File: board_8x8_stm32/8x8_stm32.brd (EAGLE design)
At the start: 100 x 100 mm, 127 parts, among them IC1 STM32F0, J1 SWD_SHROUD, Q1 BSS123, Q10 BSS84, Q11 BSS84, Q12 BSS84, Q13 BSS84, Q14 BSS84, Q15 BSS84, Q16 BSS84, Q2 BSS123, Q3 BSS123, Q4 BSS123, Q5 BSS123, Q6 BSS123, Q7 BSS123, Q8 BSS123, Q9 BSS84

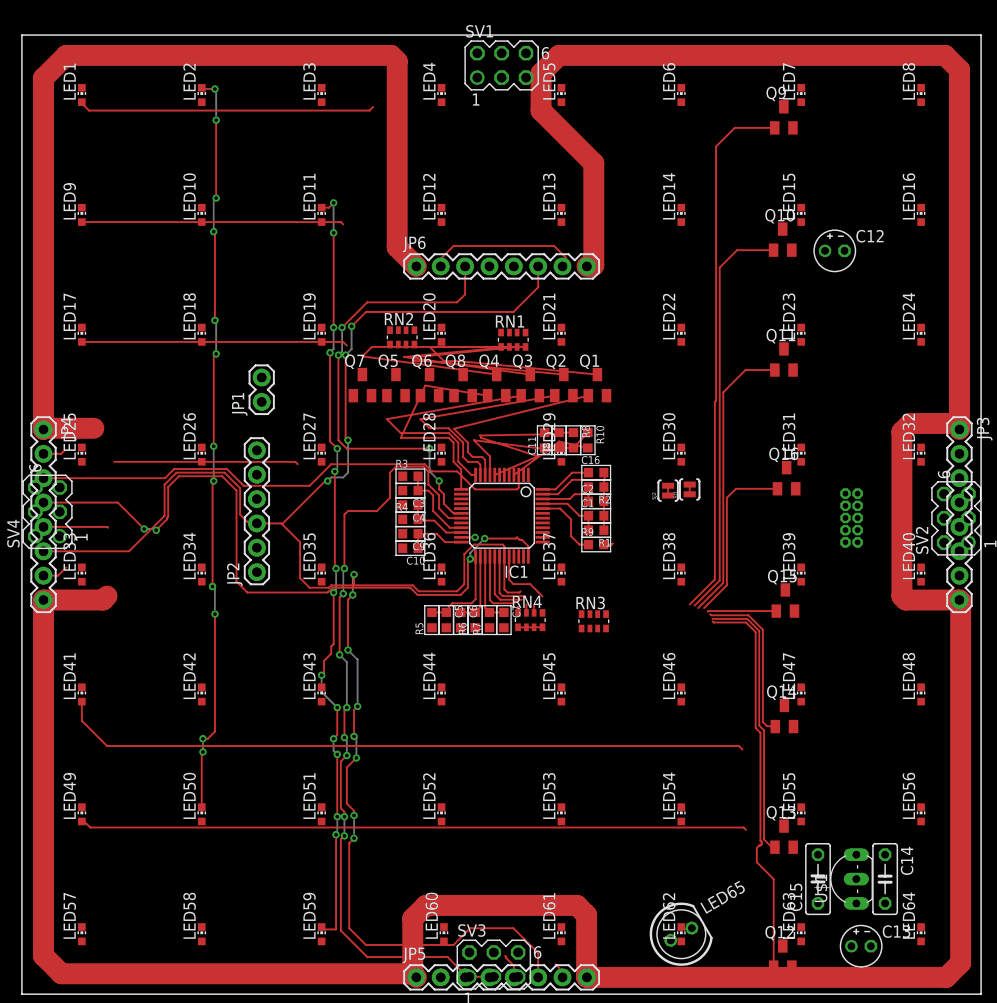
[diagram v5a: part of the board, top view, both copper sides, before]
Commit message: chnaging to combined led footprint
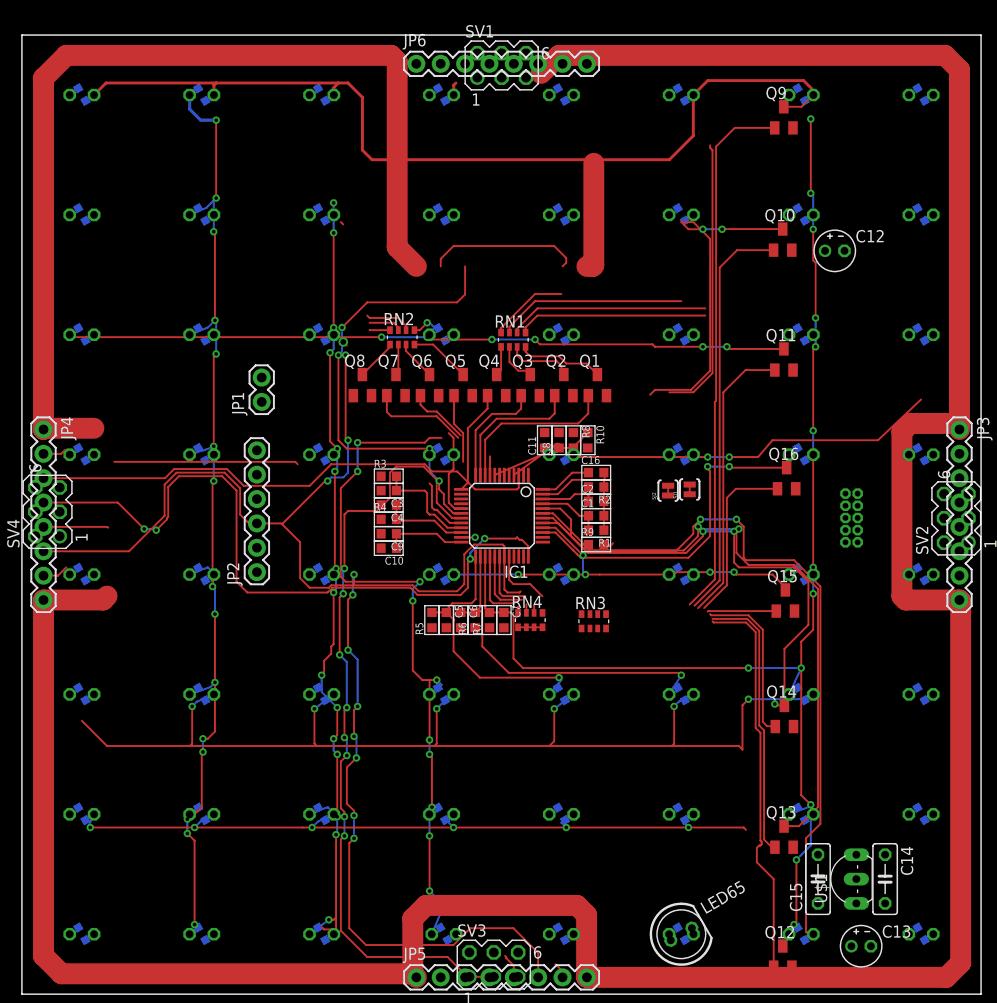
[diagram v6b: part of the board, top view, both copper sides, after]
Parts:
- LED1, LED10, LED11, LED12, LED13, LED14, LED15, LED16, LED17, LED18, LED19, LED2, LED20, LED21, LED22, LED23, LED24, LED25, LED26, LED27, LED28, LED29, LED3, LED30, LED31, LED32, LED33, LED34, LED35, LED36, LED37, LED38, LED39, LED4, LED40, LED41, LED42, LED43, LED44, LED45, LED46, LED47, LED48, LED49, LED5, LED50, LED51, LED52, LED53, LED54, LED55, LED56, LED57, LED58, LED59, LED6, LED60, LED61, LED62, LED63, LED64, LED7, LED8, LED9: device dtb:CHIP-LED0603 -> dtb:LED5MM/SMD
- moved JP6 21.1 mm to (41.1, 97.0)
- moved Q8 10.5 mm to (35.5, 63.5)
- moved Q5 7.00 mm to (46.0, 63.5)
- moved Q7 3.50 mm to (39.0, 63.5)
- moved C10 2.25 mm to (38.2, 46.5)
- moved C3 2.25 mm to (38.2, 52.5)
- moved C4 2.25 mm to (38.2, 51.0)
- moved C9 2.25 mm to (38.2, 48.0)
- moved R3 2.25 mm to (38.2, 54.0)
- moved R4 2.25 mm to (38.2, 49.5)
- flipped LED1 to the bottom
- flipped LED10 to the bottom
- flipped LED11 to the bottom
- flipped LED12 to the bottom
- flipped LED13 to the bottom
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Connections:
- net COL1: now also LED1.K, LED1.K1, LED17.K, LED17.K1, LED25.K, LED25.K1, LED33.K, LED33.K1, LED41.K, LED41.K1, LED49.K, LED49.K1, LED57.K, LED57.K1, LED9.K, LED9.K1, RN2.8; no longer LED1.C, LED17.C, LED25.C, LED33.C, LED41.C, LED49.C, LED57.C, LED9.C, RN1.5
- net COL2: now also LED10.K, LED10.K1, LED18.K, LED18.K1, LED2.K, LED2.K1, LED26.K, LED26.K1, LED34.K, LED34.K1, LED42.K, LED42.K1, LED50.K, LED50.K1, LED58.K, LED58.K1, RN2.7; no longer LED10.C, LED18.C, LED2.C, LED26.C, LED34.C, LED42.C, LED50.C, LED58.C, RN1.6
- net COL3: now also LED11.K, LED11.K1, LED19.K, LED19.K1, LED27.K, LED27.K1, LED3.K, LED3.K1, LED35.K, LED35.K1, LED43.K, LED43.K1, LED51.K, LED51.K1, LED59.K, LED59.K1, RN2.6; no longer LED11.C, LED19.C, LED27.C, LED3.C, LED35.C, LED43.C, LED51.C, LED59.C, RN1.7
- net COL4: now also LED12.K, LED12.K1, LED20.K, LED20.K1, LED28.K, LED28.K1, LED36.K, LED36.K1, LED4.K, LED4.K1, LED44.K, LED44.K1, LED52.K, LED52.K1, LED60.K, LED60.K1, RN2.5; no longer LED12.C, LED20.C, LED28.C, LED36.C, LED4.C, LED44.C, LED52.C, LED60.C, RN1.8
- net COL5: now also LED13.K, LED13.K1, LED21.K, LED21.K1, LED29.K, LED29.K1, LED37.K, LED37.K1, LED45.K, LED45.K1, LED5.K, LED5.K1, LED53.K, LED53.K1, LED61.K, LED61.K1, RN1.8; no longer LED13.C, LED21.C, LED29.C, LED37.C, LED45.C, LED5.C, LED53.C, LED61.C, RN2.8
- net COL6: now also LED14.K, LED14.K1, LED22.K, LED22.K1, LED30.K, LED30.K1, LED38.K, LED38.K1, LED46.K, LED46.K1, LED54.K, LED54.K1, LED6.K, LED6.K1, LED62.K, LED62.K1, RN1.7; no longer LED14.C, LED22.C, LED30.C, LED38.C, LED46.C, LED54.C, LED6.C, LED62.C, RN2.7
- net COL7: now also LED15.K, LED15.K1, LED23.K, LED23.K1, LED31.K, LED31.K1, LED39.K, LED39.K1, LED47.K, LED47.K1, LED55.K, LED55.K1, LED63.K, LED63.K1, LED7.K, LED7.K1, RN1.6; no longer LED15.C, LED23.C, LED31.C, LED39.C, LED47.C, LED55.C, LED63.C, LED7.C, RN2.6
- net COL8: now also LED16.K, LED16.K1, LED24.K, LED24.K1, LED32.K, LED32.K1, LED40.K, LED40.K1, LED48.K, LED48.K1, LED56.K, LED56.K1, LED64.K, LED64.K1, LED8.K, LED8.K1, RN1.5; no longer LED16.C, LED24.C, LED32.C, LED40.C, LED48.C, LED56.C, LED64.C, LED8.C, RN2.5
- net N$1: now also RN2.1; no longer RN2.4
- net N$2: now also RN2.2; no longer RN2.3
- net N$3: now also RN2.3; no longer RN2.2
- net N$4: now also RN2.4; no longer RN2.1
- net ROW1: now also LED1.A1, LED2.A1, LED3.A1, LED4.A1, LED5.A1, LED6.A1, LED7.A1, LED8.A1
- net ROW2: now also LED10.A1, LED11.A1, LED12.A1, LED13.A1, LED14.A1, LED15.A1, LED16.A1, LED9.A1
- net ROW3: now also LED17.A1, LED18.A1, LED19.A1, LED20.A1, LED21.A1, LED22.A1, LED23.A1, LED24.A1
- net ROW4: now also LED25.A1, LED26.A1, LED27.A1, LED28.A1, LED29.A1, LED30.A1, LED31.A1, LED32.A1
- net ROW5: now also LED33.A1, LED34.A1, LED35.A1, LED36.A1, LED37.A1, LED38.A1, LED39.A1, LED40.A1
- net ROW6: now also LED41.A1, LED42.A1, LED43.A1, LED44.A1, LED45.A1, LED46.A1, LED47.A1, LED48.A1
- net ROW7: now also LED49.A1, LED50.A1, LED51.A1, LED52.A1, LED53.A1, LED54.A1, LED55.A1, LED56.A1
- net ROW8: now also LED57.A1, LED58.A1, LED59.A1, LED60.A1, LED61.A1, LED62.A1, LED63.A1, LED64.A1
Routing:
- net COL7: track 7.52 -> 157.9 mm, vias 0 -> 14
- net ROW1: track 31.0 -> 130.4 mm
- net ROW6: track 72.1 -> 165.2 mm, vias 0 -> 9
- net COL4: track 6.57 -> 87.7 mm, vias 0 -> 11
- net ROW7: track 69.6 -> 145.1 mm, vias 0 -> 8
- net ROW8: track 0.00 -> 74.5 mm, vias 0 -> 2
- net COL8: track 3.69 -> 62.9 mm, vias 0 -> 2
- net ROW3: track 27.8 -> 81.6 mm, vias 0 -> 7
- net COL6: track 7.56 -> 55.6 mm, vias 0 -> 1
- net ROW5: track 0.00 -> 43.6 mm, vias 0 -> 6
- net COL2: track 84.4 -> 123.2 mm, vias 12 -> 15
- net ROW4: track 19.2 -> 54.3 mm, vias 0 -> 2
- net COL5: track 9.76 -> 36.8 mm, vias 0 -> 1
- net G_UART: track 185.5 -> 158.9 mm, vias 12 -> 11
- net N$5: track 29.0 -> 3.07 mm
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
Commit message: routing...
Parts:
- removed LED65: (no value), dtb:LED5MM
- removed LED66: (no value), dtb:LED10MM
- removed SV1, SV2, SV3, SV4: (no value), con-lstb:MA03-2
- moved C13 24.1 mm to (73.8, 24.8), turned to 90 degrees
- moved RN4 21.6 mm to (74.2, 35.0)
- moved Q12 18.3 mm to (61.8, 9.42)
- moved Q14 18.2 mm to (61.8, 25.0)
- moved Q15 18.1 mm to (61.9, 37.3)
- moved Q13 17.6 mm to (62.0, 14.7)
- moved C12 11.3 mm to (73.8, 75.0), turned to 90 degrees
- moved RN3 5.75 mm to (53.9, 38.9)
- moved R1 3.91 mm to (62.9, 50.9), turned to 0 degrees
- moved C2 3.16 mm to (62.9, 52.4), turned to 180 degrees
- moved Q16 2.24 mm to (77.7, 52.8)
- moved R9 2.00 mm to (59.9, 48.9)
- moved Q10 1.82 mm to (77.6, 78.2)
- moved Q11 1.82 mm to (77.7, 65.7)
- moved C1 1.00 mm to (59.9, 50.9)
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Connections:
- net +3V3: no longer SV2.2, SV4.2
- net +5V: no longer SV2.6, SV4.6
- net COMMS_DOWN: no longer SV3.3
- net COMMS_LEFT: no longer SV4.3
- net COMMS_RIGHT: no longer SV2.3
- net COMMS_UP: no longer SV1.3
- net GND: no longer SV1.1, SV2.1, SV3.1, SV4.1
- net G_UART: no longer SV1.4, SV2.4, SV3.4, SV4.4
- net RFET1: now also IC1.33; no longer IC1.29
- net RFET2: now also SJ1.2; no longer IC1.30, JP2.2
- net RFET3: now also SJ2.2; no longer IC1.28
- net RFET4: now also IC1.38; no longer IC1.32
- net RFET5: now also IC1.29, RN3.7; no longer IC1.33, RN3.5
- net RFET6: now also IC1.30, JP2.2; no longer SJ1.2
- net RFET7: now also IC1.28, RN3.8; no longer RN3.7, SJ2.2
- net RFET8: now also IC1.32, RN3.5; no longer IC1.38, RN3.8
- net SHIFT_LEFT: no longer SV4.5
- net SHIFT_RIGHT: no longer SV2.5
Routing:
- net COL1: track 10.1 -> 112.3 mm
- net COL8: track 62.9 -> 146.6 mm
- net ROW8: track 74.5 -> 152.1 mm, vias 2 -> 1
- net +5V: track 421.0 -> 494.9 mm, vias 0 -> 6
- net ROW2: track 36.0 -> 107.9 mm, vias 2 -> 7
- net COL7: track 157.9 -> 100.8 mm, vias 14 -> 1
- net COL5: track 36.8 -> 91.8 mm, vias 1 -> 2
- net COL6: track 55.6 -> 109.4 mm, vias 1 -> 2
- net COL2: track 123.2 -> 171.7 mm, vias 15 -> 8
- net RFET2: track 50.2 -> 3.71 mm
- net ROW5: track 43.6 -> 89.2 mm
- net ROW1: track 130.4 -> 85.2 mm
- net RFET1: track 63.7 -> 22.4 mm
- net ROW6: track 165.2 -> 124.0 mm, vias 9 -> 8
- net RFET5: track 7.18 -> 34.0 mm, vias 0 -> 2
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
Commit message: more routig..
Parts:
- moved JP1 68.3 mm to (88.5, 36.5), turned to 0 degrees
- moved C15 50.5 mm to (82.0, 62.5), turned to 270 degrees
- moved U$1 50.5 mm to (86.0, 62.5)
- moved C14 50.3 mm to (89.0, 62.2)
- moved JP2 47.1 mm to (71.0, 36.5), turned to 0 degrees
- moved R9 34.2 mm to (90.1, 32.9), turned to 180 degrees
- moved RN4 19.0 mm to (74.0, 54.0), turned to 90 degrees
- moved C13 12.8 mm to (61.0, 24.2), turned to 180 degrees
- moved RN3 9.71 mm to (61.9, 33.4), turned to 90 degrees
- moved R10 7.32 mm to (51.8, 56.8)
- moved C11 5.10 mm to (49.5, 56.8), turned to 270 degrees
- moved Q14 4.37 mm to (60.8, 29.2)
- moved Q13 2.50 mm to (62.0, 17.2)
- moved C8 2.24 mm to (54.0, 58.8), turned to 180 degrees
- moved SJ1 2.07 mm to (67.8, 51.8)
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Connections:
- net COL1: now also C6.1, IC1.26, R6.2; no longer C1.1, IC1.45, R1.2
- net COL2: now also C5.1, IC1.25, R5.2; no longer C2.1, IC1.46, R2.2
- net COL5: now also C7.1, IC1.27, R7.2; no longer C5.1, IC1.25, R5.2
- net COL6: now also C2.1, IC1.46, R2.2; no longer C6.1, IC1.26, R6.2
- net COL7: now also C1.1, IC1.45, R1.2; no longer C7.1, IC1.27, R7.2
- net RFET1: now also RN4.5; no longer RN4.7
- net RFET3: now also RN4.7; no longer RN4.8
- net RFET4: now also RN4.8; no longer RN4.5
- net RFET5: now also RN3.5; no longer RN3.7
- net RFET6: now also RN3.8; no longer RN3.6
- net RFET7: now also RN3.7; no longer RN3.8
- net RFET8: now also RN3.6; no longer RN3.5
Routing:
- net +3V3: track 4.46 -> 477.8 mm, vias 0 -> 22
- net G_UART: track 156.1 -> 280.9 mm, vias 7 -> 10
- net COL5: track 91.8 -> 198.3 mm, vias 2 -> 8
- net ROW4: track 48.6 -> 153.3 mm, vias 4 -> 8
- net ROW5: track 89.2 -> 173.7 mm, vias 6 -> 9
- net COL1: track 112.3 -> 190.7 mm, vias 0 -> 5
- net ROW1: track 85.2 -> 161.5 mm, vias 0 -> 5
- net RFET1: track 22.4 -> 93.9 mm, vias 0 -> 8
- net COL7: track 100.8 -> 160.0 mm, vias 1 -> 4
- net N$9: track 0.00 -> 55.6 mm, vias 0 -> 4
- net COMMS_RIGHT: track 0.00 -> 54.7 mm, vias 0 -> 4
- net NRST: track 0.00 -> 50.1 mm, vias 0 -> 6
- net +5V: track 494.9 -> 543.7 mm, vias 6 -> 10
- net ROW3: track 103.1 -> 149.7 mm, vias 9 -> 8
- net SHIFT_RIGHT: track 17.3 -> 61.3 mm
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- added copper zone on layer 16, net GND
